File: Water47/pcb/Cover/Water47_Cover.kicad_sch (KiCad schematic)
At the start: 4 parts

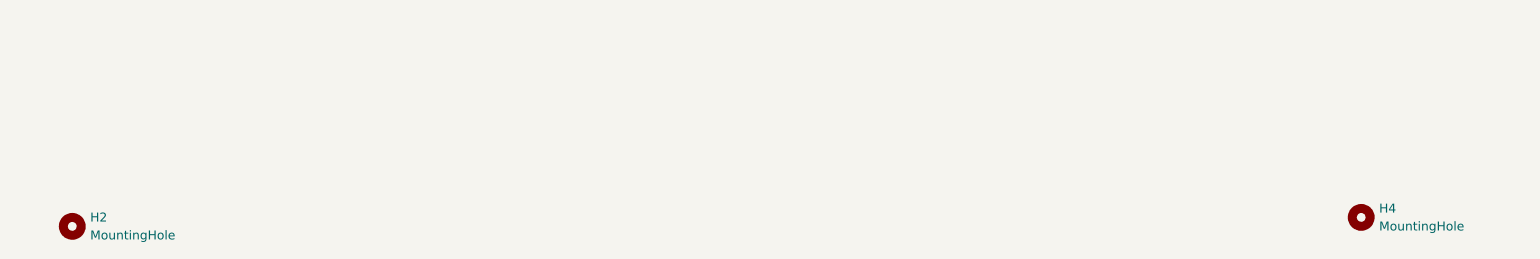
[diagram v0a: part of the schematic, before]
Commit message: feat: change mounting hole
PCB : Hex
Others : Round
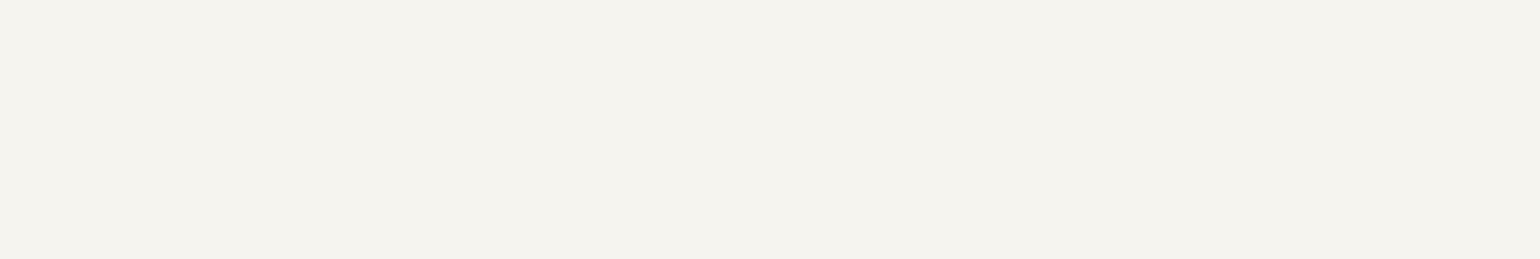
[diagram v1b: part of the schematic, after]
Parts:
- removed H2, H4: MountingHole, kbd_Hole:m2_Screw_Hole, symbol Mechanical:MountingHole
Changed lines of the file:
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@@
-    )
-  )
-  (symbol (lib_id "Mechanical:MountingHole") (at 29.21 218.44 0) (unit 1)
-    (in_bom yes) (on_board yes) (fields_autoplaced)
-    (property "Reference" "H2" (id 0) (at 31.75 217.1699 0)
-      (effects (font (size 1.27 1.27)) (justify left))
-    )
-    (property "Value" "MountingHole" (id 1) (at 31.75 219.7099 0)
-      (effects (font (size 1.27 1.27)) (justify left))
-    )
-    (property "Footprint" "kbd_Hole:m2_Screw_Hole" (id 2) (at 29.21 218.44 0)
-      (effects (font (size 1.27 1.27)) hide)
-    )
-    (property "Datasheet" "~" (id 3) (at 29.21 218.44 0)
-      (effects (font (size 1.27 1.27)) hide)
-    )
-  )
-  (symbol (lib_id "Mechanical:MountingHole") (at 212.09 217.17 0) (unit 1)
-    (in_bom yes) (on_board yes) (fields_autoplaced)
-    (property "Reference" "H4" (id 0) (at 214.63 215.8999 0)
-      (effects (font (size 1.27 1.27)) (justify left))
-    )
-    (property "Value" "MountingHole" (id 1) (at 214.63 218.4399 0)
-      (effects (font (size 1.27 1.27)) (justify left))
-    )
-    (property "Footprint" "kbd_Hole:m2_Screw_Hole" (id 2) (at 212.09 217.17 0)
-      (effects (font (size 1.27 1.27)) hide)
-    )
-    (property "Datasheet" "~" (id 3) (at 212.09 217.17 0)
-      (effects (font (size 1.27 1.27)) hide)
     )
   )
@@
       (reference "H1") (unit 1) (value "MountingHole") (footprint "kbd_Hole:m2_Screw_Hole")
     )
-    (path "/bbde9b31-2ca1-42cc-a23f-bd08fc375c76"
-      (reference "H2") (unit 1) (value "MountingHole") (footprint "kbd_Hole:m2_Screw_Hole")
-    )
     (path "/f64ccafc-8d73-4e0d-a0a9-52c38f87dc6c"
       (reference "H3") (unit 1) (value "MountingHole") (footprint "kbd_Hole:m2_Screw_Hole")
     )
-    (path "/caa5335b-ab47-478f-b510-96296c076797"
-      (reference "H4") (unit 1) (value "MountingHole") (footprint "kbd_Hole:m2_Screw_Hole")
-    )
   )

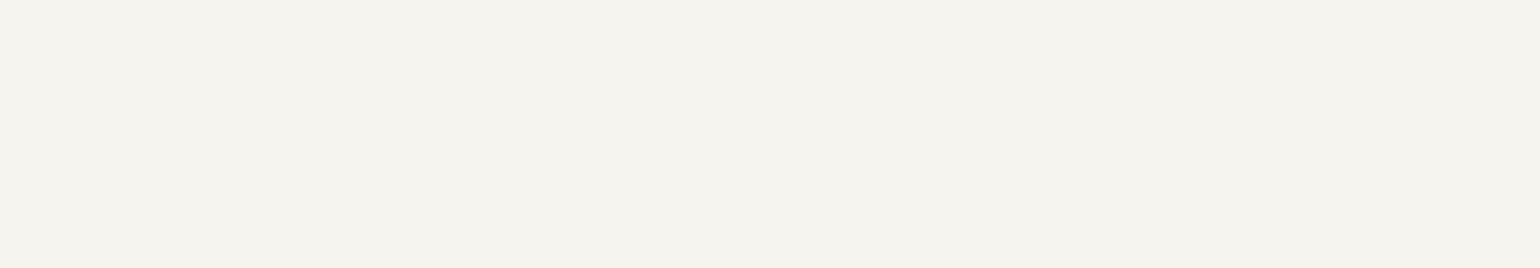
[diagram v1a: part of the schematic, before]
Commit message: feat: add mounting holes
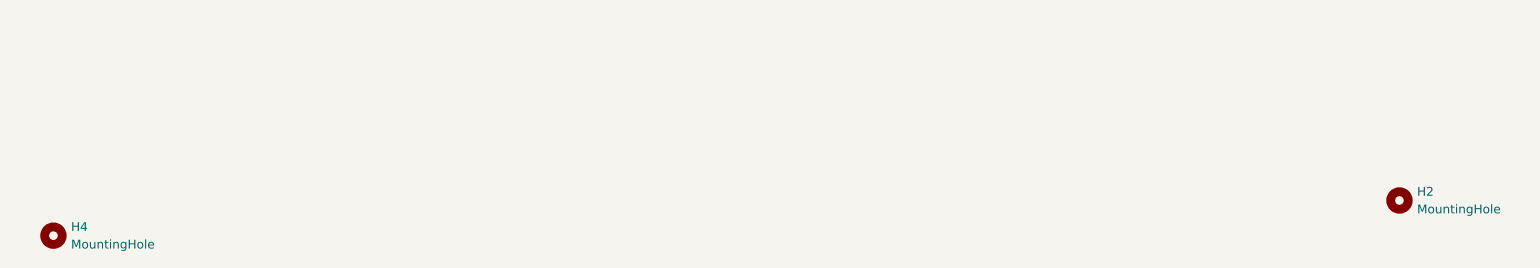
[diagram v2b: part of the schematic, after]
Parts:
- added H2, H4: MountingHole, kbd_Hole:m2_Screw_Hole, symbol Mechanical:MountingHole
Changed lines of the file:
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@@
 (kicad_sch (version 20211123) (generator eeschema)
   (paper "A3")
+  (symbol (lib_id "Mechanical:MountingHole") (at 26.67 167.64 0) (unit 1)
+    (in_bom yes) (on_board yes) (fields_autoplaced)
+    (property "Reference" "H4" (id 0) (at 29.21 166.3699 0)
+      (effects (font (size 1.27 1.27)) (justify left))
+    )
+    (property "Value" "MountingHole" (id 1) (at 29.21 168.9099 0)
+      (effects (font (size 1.27 1.27)) (justify left))
+    )
+    (property "Footprint" "kbd_Hole:m2_Screw_Hole" (id 2) (at 26.67 167.64 0)
+      (effects (font (size 1.27 1.27)) hide)
+    )
+    (property "Datasheet" "~" (id 3) (at 26.67 167.64 0)
+      (effects (font (size 1.27 1.27)) hide)
+    )
+  )
   (symbol (lib_id "Mechanical:MountingHole") (at 22.86 68.58 0) (unit 1)
     (in_bom yes) (on_board yes) (fields_autoplaced)
@@
     )
     (property "Datasheet" "~" (id 3) (at 22.86 68.58 0)
+      (effects (font (size 1.27 1.27)) hide)
+    )
+  )
+  (symbol (lib_id "Mechanical:MountingHole") (at 220.98 162.56 0) (unit 1)
+    (in_bom yes) (on_board yes) (fields_autoplaced)
+    (property "Reference" "H2" (id 0) (at 223.52 161.2899 0)
+      (effects (font (size 1.27 1.27)) (justify left))
+    )
+    (property "Value" "MountingHole" (id 1) (at 223.52 163.8299 0)
+      (effects (font (size 1.27 1.27)) (justify left))
+    )
+    (property "Footprint" "kbd_Hole:m2_Screw_Hole" (id 2) (at 220.98 162.56 0)
+      (effects (font (size 1.27 1.27)) hide)
+    )
+    (property "Datasheet" "~" (id 3) (at 220.98 162.56 0)
       (effects (font (size 1.27 1.27)) hide)
     )
@@
       (reference "H1") (unit 1) (value "MountingHole") (footprint "kbd_Hole:m2_Screw_Hole")
     )
+    (path "/e4212f01-80a6-4002-8033-8a2c8a060b8a"
+      (reference "H2") (unit 1) (value "MountingHole") (footprint "kbd_Hole:m2_Screw_Hole")
+    )
     (path "/f64ccafc-8d73-4e0d-a0a9-52c38f87dc6c"
       (reference "H3") (unit 1) (value "MountingHole") (footprint "kbd_Hole:m2_Screw_Hole")
     )
+    (path "/124e03b5-b9bd-484e-96ec-08f232e7e039"
+      (reference "H4") (unit 1) (value "MountingHole") (footprint "kbd_Hole:m2_Screw_Hole")
+    )
   )

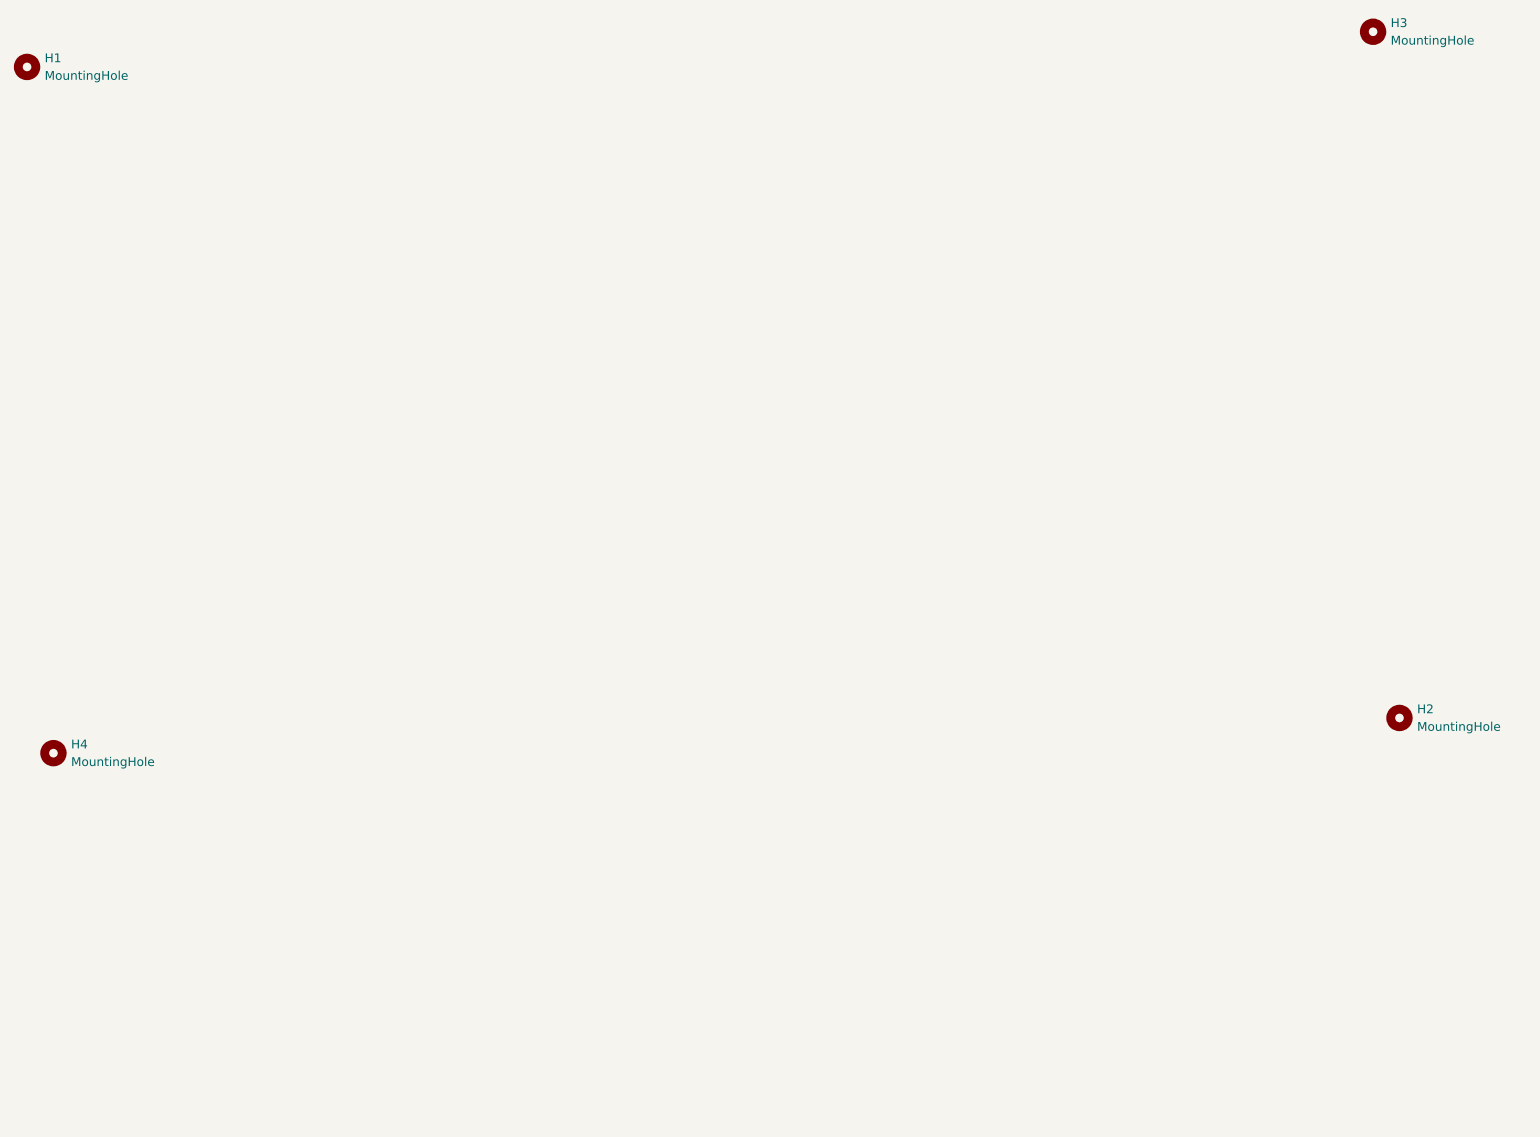
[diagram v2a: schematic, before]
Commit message: feat: add mounting hole, set gerber path
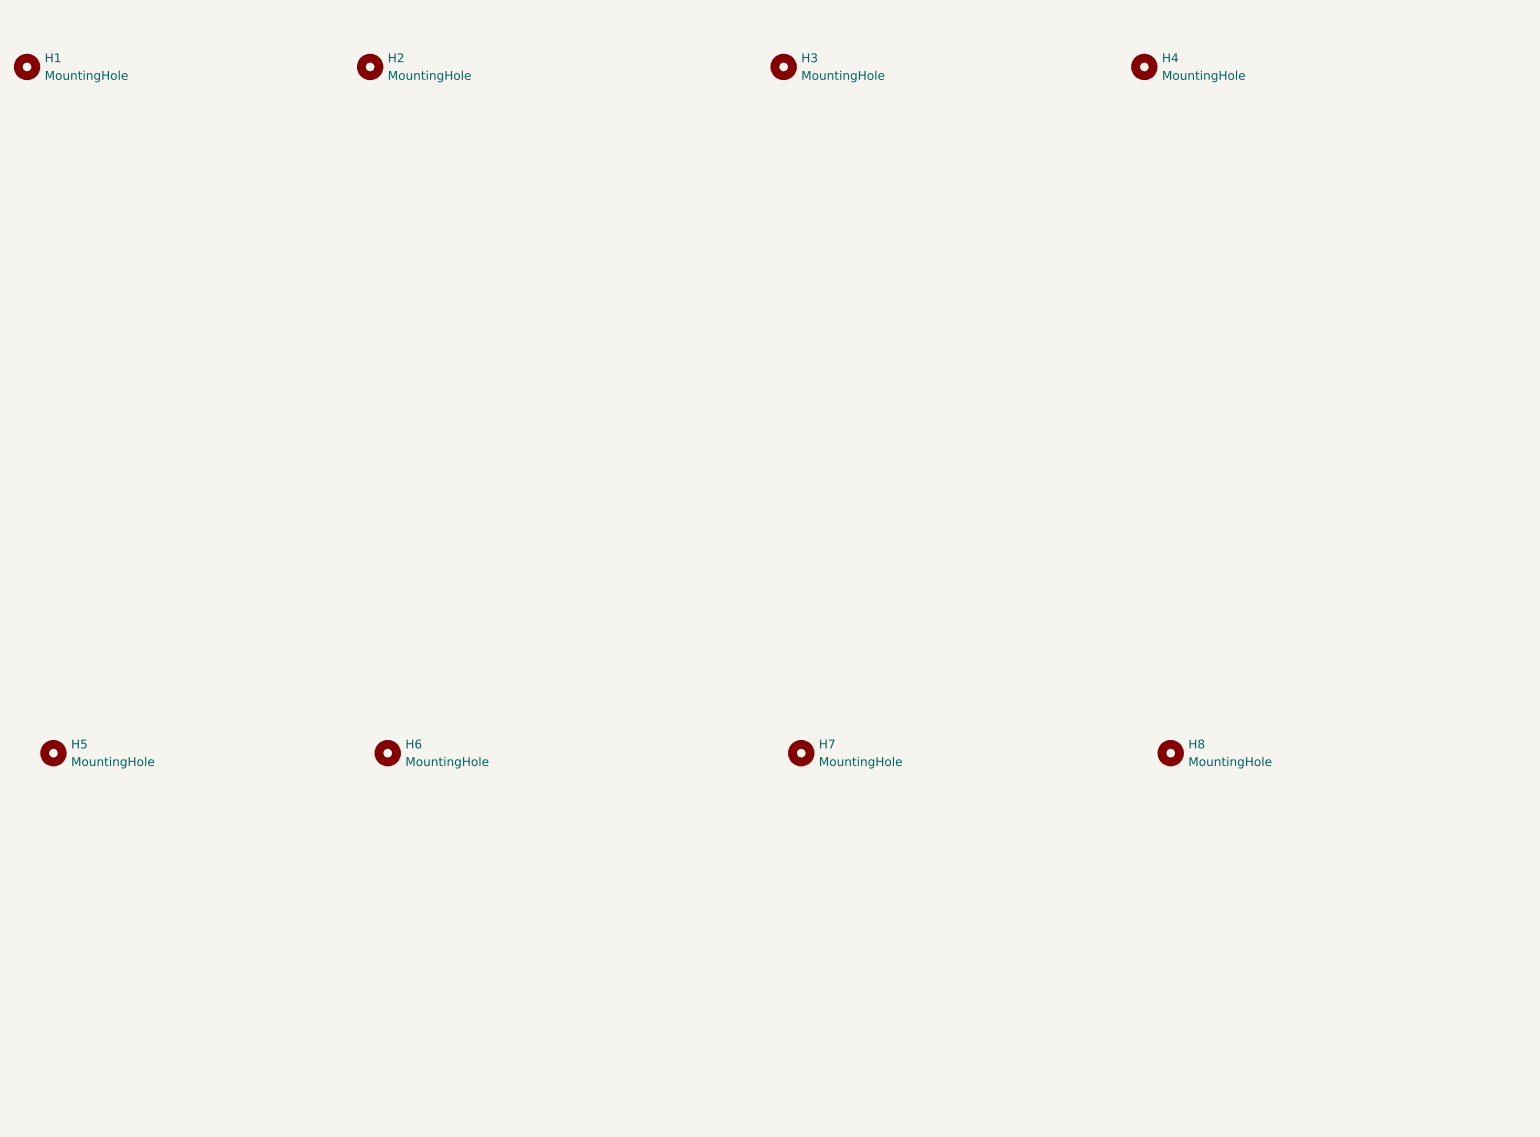
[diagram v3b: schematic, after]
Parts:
- added H2, H3, H6, H7: MountingHole, kbd_Hole:m2_Screw_Hole, symbol Mechanical:MountingHole
- renumbered H3 to H4, H4 to H5, H2 to H8
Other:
- moved on the sheet: H4, H8
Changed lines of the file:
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@@
   (symbol (lib_id "Mechanical:MountingHole") (at 26.67 167.64 0) (unit 1)
     (in_bom yes) (on_board yes) (fields_autoplaced)
-    (property "Reference" "H4" (id 0) (at 29.21 166.3699 0)
+    (property "Reference" "H5" (id 0) (at 29.21 166.3699 0)
       (effects (font (size 1.27 1.27)) (justify left))
     )
@@
     )
   )
-  (symbol (lib_id "Mechanical:MountingHole") (at 220.98 162.56 0) (unit 1)
+  (symbol (lib_id "Mechanical:MountingHole") (at 132.08 68.58 0) (unit 1)
     (in_bom yes) (on_board yes) (fields_autoplaced)
-    (property "Reference" "H2" (id 0) (at 223.52 161.2899 0)
+    (property "Reference" "H3" (id 0) (at 134.62 67.3099 0)
       (effects (font (size 1.27 1.27)) (justify left))
     )
-    (property "Value" "MountingHole" (id 1) (at 223.52 163.8299 0)
+    (property "Value" "MountingHole" (id 1) (at 134.62 69.8499 0)
       (effects (font (size 1.27 1.27)) (justify left))
     )
-    (property "Footprint" "kbd_Hole:m2_Screw_Hole" (id 2) (at 220.98 162.56 0)
+    (property "Footprint" "kbd_Hole:m2_Screw_Hole" (id 2) (at 132.08 68.58 0)
       (effects (font (size 1.27 1.27)) hide)
     )
-    (property "Datasheet" "~" (id 3) (at 220.98 162.56 0)
+    (property "Datasheet" "~" (id 3) (at 132.08 68.58 0)
       (effects (font (size 1.27 1.27)) hide)
     )
   )
-  (symbol (lib_id "Mechanical:MountingHole") (at 217.17 63.5 0) (unit 1)
+  (symbol (lib_id "Mechanical:MountingHole") (at 72.39 68.58 0) (unit 1)
     (in_bom yes) (on_board yes) (fields_autoplaced)
-    (property "Reference" "H3" (id 0) (at 219.71 62.2299 0)
+    (property "Reference" "H2" (id 0) (at 74.93 67.3099 0)
       (effects (font (size 1.27 1.27)) (justify left))
     )
-    (property "Value" "MountingHole" (id 1) (at 219.71 64.7699 0)
+    (property "Value" "MountingHole" (id 1) (at 74.93 69.8499 0)
       (effects (font (size 1.27 1.27)) (justify left))
     )
-    (property "Footprint" "kbd_Hole:m2_Screw_Hole" (id 2) (at 217.17 63.5 0)
+    (property "Footprint" "kbd_Hole:m2_Screw_Hole" (id 2) (at 72.39 68.58 0)
       (effects (font (size 1.27 1.27)) hide)
     )
-    (property "Datasheet" "~" (id 3) (at 217.17 63.5 0)
+    (property "Datasheet" "~" (id 3) (at 72.39 68.58 0)
+      (effects (font (size 1.27 1.27)) hide)
+    )
+  )
+  (symbol (lib_id "Mechanical:MountingHole") (at 74.93 167.64 0) (unit 1)
+    (in_bom yes) (on_board yes) (fields_autoplaced)
+    (property "Reference" "H6" (id 0) (at 77.47 166.3699 0)
+      (effects (font (size 1.27 1.27)) (justify left))
+    )
+    (property "Value" "MountingHole" (id 1) (at 77.47 168.9099 0)
+      (effects (font (size 1.27 1.27)) (justify left))
+    )
+    (property "Footprint" "kbd_Hole:m2_Screw_Hole" (id 2) (at 74.93 167.64 0)
+      (effects (font (size 1.27 1.27)) hide)
+    )
+    (property "Datasheet" "~" (id 3) (at 74.93 167.64 0)
+      (effects (font (size 1.27 1.27)) hide)
+    )
+  )
+  (symbol (lib_id "Mechanical:MountingHole") (at 134.62 167.64 0) (unit 1)
+    (in_bom yes) (on_board yes) (fields_autoplaced)
+    (property "Reference" "H7" (id 0) (at 137.16 166.3699 0)
+      (effects (font (size 1.27 1.27)) (justify left))
+    )
+    (property "Value" "MountingHole" (id 1) (at 137.16 168.9099 0)
+      (effects (font (size 1.27 1.27)) (justify left))
+    )
+    (property "Footprint" "kbd_Hole:m2_Screw_Hole" (id 2) (at 134.62 167.64 0)
+      (effects (font (size 1.27 1.27)) hide)
+    )
+    (property "Datasheet" "~" (id 3) (at 134.62 167.64 0)
+      (effects (font (size 1.27 1.27)) hide)
+    )
+  )
+  (symbol (lib_id "Mechanical:MountingHole") (at 187.96 167.64 0) (unit 1)
+    (in_bom yes) (on_board yes) (fields_autoplaced)
+    (property "Reference" "H8" (id 0) (at 190.5 166.3699 0)
+      (effects (font (size 1.27 1.27)) (justify left))
+    )
+    (property "Value" "MountingHole" (id 1) (at 190.5 168.9099 0)
+      (effects (font (size 1.27 1.27)) (justify left))
+    )
+    (property "Footprint" "kbd_Hole:m2_Screw_Hole" (id 2) (at 187.96 167.64 0)
+      (effects (font (size 1.27 1.27)) hide)
+    )
+    (property "Datasheet" "~" (id 3) (at 187.96 167.64 0)
+      (effects (font (size 1.27 1.27)) hide)
+    )
+  )
+  (symbol (lib_id "Mechanical:MountingHole") (at 184.15 68.58 0) (unit 1)
+    (in_bom yes) (on_board yes) (fields_autoplaced)
+    (property "Reference" "H4" (id 0) (at 186.69 67.3099 0)
+      (effects (font (size 1.27 1.27)) (justify left))
+    )
+    (property "Value" "MountingHole" (id 1) (at 186.69 69.8499 0)
+      (effects (font (size 1.27 1.27)) (justify left))
+    )
+    (property "Footprint" "kbd_Hole:m2_Screw_Hole" (id 2) (at 184.15 68.58 0)
+      (effects (font (size 1.27 1.27)) hide)
+    )
+    (property "Datasheet" "~" (id 3) (at 184.15 68.58 0)
       (effects (font (size 1.27 1.27)) hide)
     )
@@
       (reference "H1") (unit 1) (value "MountingHole") (footprint "kbd_Hole:m2_Screw_Hole")
     )
-    (path "/e4212f01-80a6-4002-8033-8a2c8a060b8a"
+    (path "/b90aac2b-b731-46d8-baa7-2e9cb0936327"
       (reference "H2") (unit 1) (value "MountingHole") (footprint "kbd_Hole:m2_Screw_Hole")
     )
-    (path "/f64ccafc-8d73-4e0d-a0a9-52c38f87dc6c"
+    (path "/480b1526-3531-48e5-bc84-299e565ac2bb"
       (reference "H3") (unit 1) (value "MountingHole") (footprint "kbd_Hole:m2_Screw_Hole")
     )
-    (path "/124e03b5-b9bd-484e-96ec-08f232e7e039"
+    (path "/f64ccafc-8d73-4e0d-a0a9-52c38f87dc6c"
       (reference "H4") (unit 1) (value "MountingHole") (footprint "kbd_Hole:m2_Screw_Hole")
     )
+    (path "/124e03b5-b9bd-484e-96ec-08f232e7e039"
+      (reference "H5") (unit 1) (value "MountingHole") (footprint "kbd_Hole:m2_Screw_Hole")
+    )
+    (path "/c9916530-2ff3-4df4-94fa-8bedc51ef2bc"
+      (reference "H6") (unit 1) (value "MountingHole") (footprint "kbd_Hole:m2_Screw_Hole")
+    )
+    (path "/dba86d56-7c7a-4ce3-b99e-50d5eada9c92"
+      (reference "H7") (unit 1) (value "MountingHole") (footprint "kbd_Hole:m2_Screw_Hole")
+    )
+    (path "/e4212f01-80a6-4002-8033-8a2c8a060b8a"
+      (reference "H8") (unit 1) (value "MountingHole") (footprint "kbd_Hole:m2_Screw_Hole")
+    )
   )
